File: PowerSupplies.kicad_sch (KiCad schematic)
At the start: 10 parts, among them U5 XL1509-3.3, U7 AP2112K-1.8

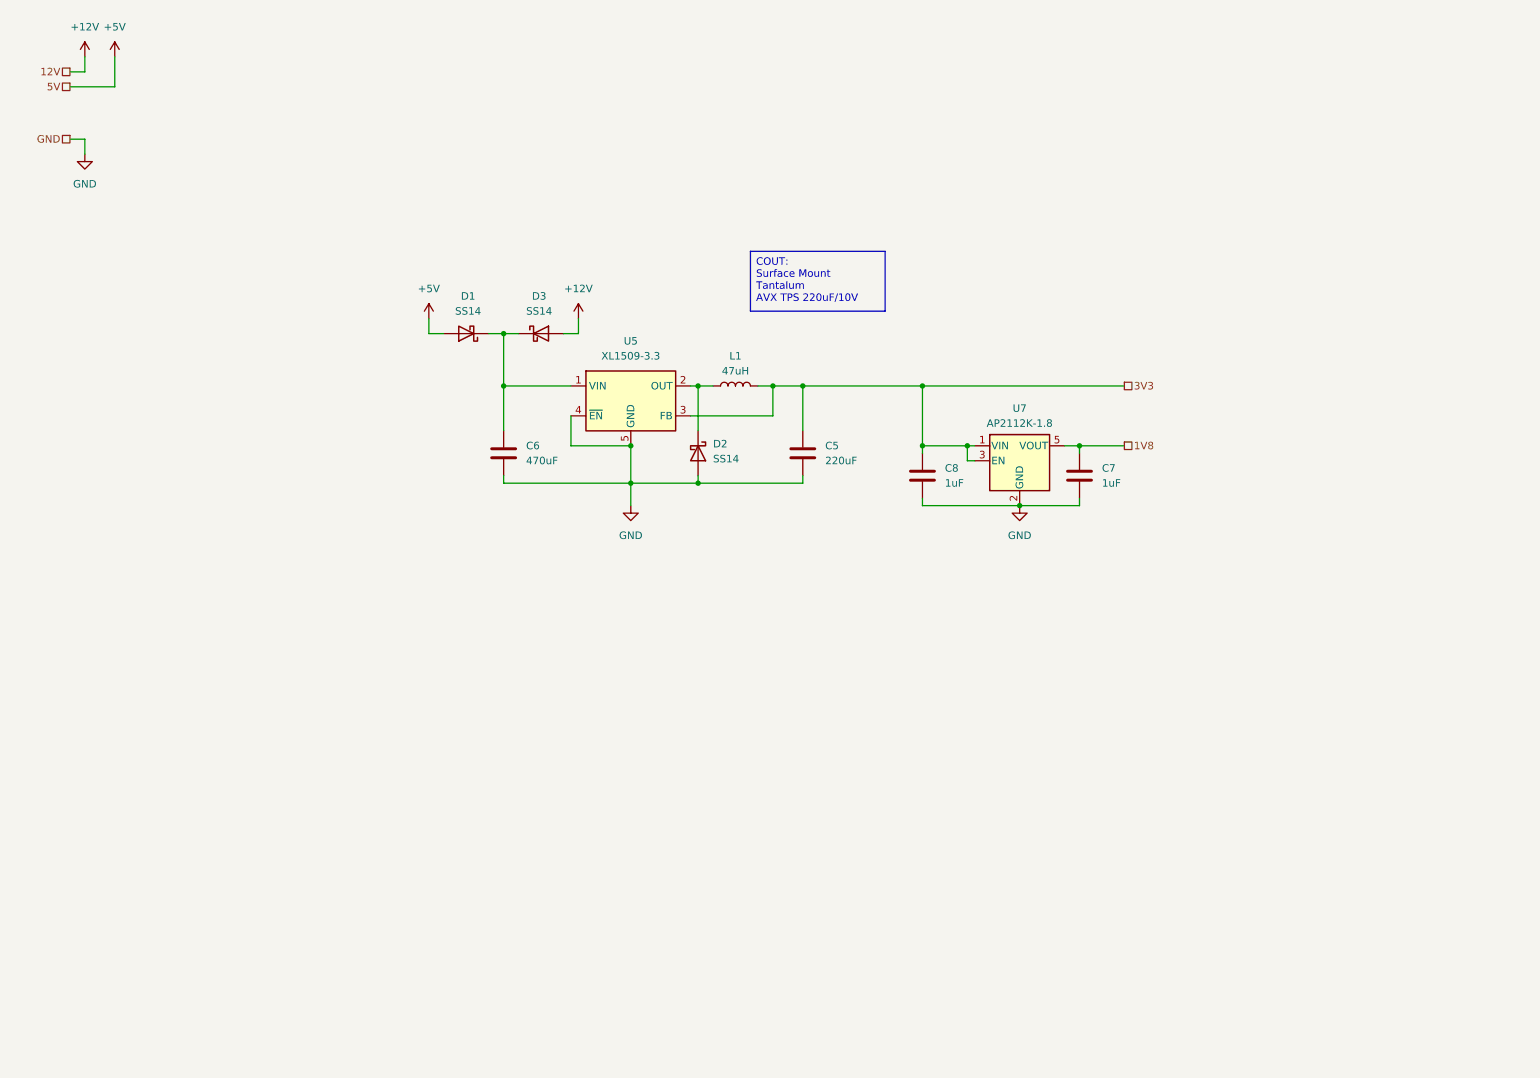
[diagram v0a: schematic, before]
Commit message: full initial power scheme
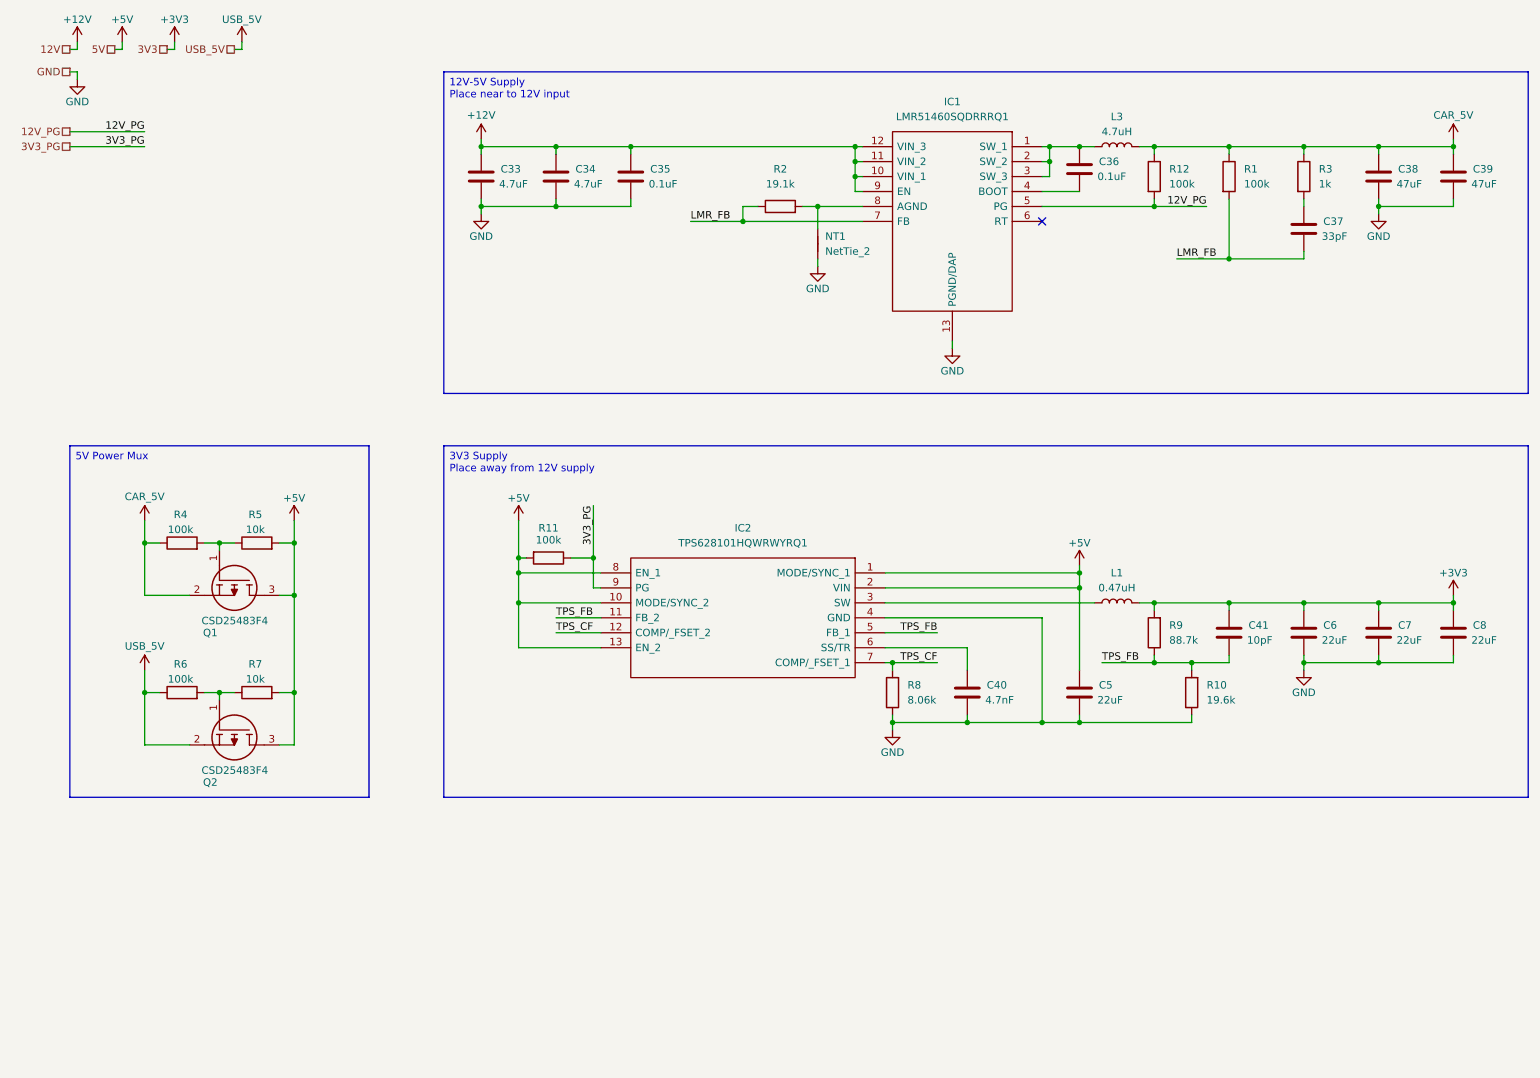
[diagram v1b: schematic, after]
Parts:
- removed D1, D2, D3: SS14, Diode_SMD:D_SMA, symbol Diode:SS14
- removed U5: XL1509-3.3, Package_SO:SOIC-8_3.9x4.9mm_P1.27mm, symbol Regulator_Switching:XL1509-3.3
- removed U7: AP2112K-1.8, Package_TO_SOT_SMD:SOT-23-5, symbol Regulator_Linear:AP2112K-1.8
- added C33, C34: 4.7uF, Capacitor_SMD:C_1210_3225Metric_Pad1.33x2.70mm_HandSolder, symbol Device:C
- added C35: 0.1uF, Capacitor_SMD:C_0603_1608Metric_Pad1.08x0.95mm_HandSolder, symbol Device:C
- added C36: 0.1uF, Capacitor_SMD:C_0402_1005Metric_Pad0.74x0.62mm_HandSolder, symbol Device:C
- added C37: 33pF, Capacitor_SMD:C_0402_1005Metric_Pad0.74x0.62mm_HandSolder, symbol Device:C
- added C38, C39: 47uF, Capacitor_SMD:C_1210_3225Metric_Pad1.33x2.70mm_HandSolder, symbol Device:C
- added C40: 4.7nF, Capacitor_SMD:C_0402_1005Metric_Pad0.74x0.62mm_HandSolder, symbol Device:C
- added C41: 10pF, Capacitor_SMD:C_0402_1005Metric_Pad0.74x0.62mm_HandSolder, symbol Device:C
- added IC1: LMR51460SQDRRRQ1, SON50P300X300X80-13N-D, symbol SamacSys_Parts:LMR51460SQDRRRQ1
- added IC2: TPS628101HQWRWYRQ1, SamacSys_Parts:TPS6281008QWRWYRQ1, symbol SamacSys_Parts:TPS62810QWRWYRQ1
- added L3: 4.7uH, Inductor_SMD:L_Coilcraft_XAL7030-472, symbol Device:L
- added NT1: NetTie_2, symbol Device:NetTie_2
- added Q1, Q2: CSD25483F4, SamacSys_Parts:CSD25483F4T, symbol SamacSys_Parts:CSD25483F4T
- added R1, R11, R12, R4, R6: 100k, Resistor_SMD:R_0402_1005Metric_Pad0.72x0.64mm_HandSolder, symbol Device:R
- added R10: 19.6k, Resistor_SMD:R_0402_1005Metric_Pad0.72x0.64mm_HandSolder, symbol Device:R
- added R2: 19.1k, Resistor_SMD:R_0402_1005Metric_Pad0.72x0.64mm_HandSolder, symbol Device:R
- added R3: 1k, Resistor_SMD:R_0402_1005Metric_Pad0.72x0.64mm_HandSolder, symbol Device:R
- added R5, R7: 10k, Resistor_SMD:R_0402_1005Metric_Pad0.72x0.64mm_HandSolder, symbol Device:R
- added R8: 8.06k, Resistor_SMD:R_0402_1005Metric_Pad0.72x0.64mm_HandSolder, symbol Device:R
- added R9: 88.7k, Resistor_SMD:R_0402_1005Metric_Pad0.72x0.64mm_HandSolder, symbol Device:R
- C5: value 220uF -> 22uF; footprint Capacitor_SMD:C_0603_1608Metric -> Inductor_SMD:L_1206_3216Metric_Pad1.22x1.90mm_HandSolder
- C6: value 470uF -> 22uF; footprint Capacitor_SMD:C_0603_1608Metric -> Inductor_SMD:L_1206_3216Metric_Pad1.22x1.90mm_HandSolder
- C7: value 1uF -> 22uF; footprint Capacitor_SMD:C_0603_1608Metric -> Inductor_SMD:L_1206_3216Metric_Pad1.22x1.90mm_HandSolder
- C8: value 1uF -> 22uF; footprint Capacitor_SMD:C_0603_1608Metric -> Capacitor_SMD:C_0603_1608Metric_Pad1.08x0.95mm_HandSolder
- L1: value 47uH -> 0.47uH; footprint Inductor_SMD:L_Sunlord_SWPA4030S -> INDPM7066X240N
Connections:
- net 1V8 is gone; now on net +3V3: C7.1
- net +12V: now also C33.1, C34.1, C35.1, IC1.10 (VIN_1), IC1.11 (VIN_2), IC1.12 (VIN_3), IC1.9 (EN)
- net +5V: now also C5.1, IC2.1 (MODE/SYNC_1), IC2.10 (MODE/SYNC_2), IC2.13 (EN_2), IC2.2 (VIN), IC2.8 (EN_1), Q1.3, Q2.3, R11.2, R5.2, R7.2
- net GND: now also C33.2, C34.2, C35.2, C38.2, C39.2, C40.2, IC1.13 (PGND/DAP), IC2.4 (GND), NT1.1, R10.1, R8.1
- net +3V3: now reaches C6.1
- net +3V3: now also C8.1, L1.2, C41.1, R9.2
- net at L1.1: now also IC2.3 (SW)
- removed net 3V3: C5.1, C8.1, L1.2
- new net: Q2.1, R6.2, R7.1
- new net: C37.1, R3.2
- new net: IC1.8 (AGND), NT1.2, R2.2
- new net: Q1.1, R4.2, R5.1
- new net: C36.1, IC1.1 (SW_1), IC1.2 (SW_2), IC1.3 (SW_3), L3.1
- new net: C36.2, IC1.4 (BOOT)
- new net: C40.1, IC2.6 (SS/TR)
- new net 12V_PG: IC1.5 (PG), R12.2
- new net 3V3_PG: IC2.9 (PG), R11.1
- new net CAR_5V: C38.1, C39.1, L3.2, Q1.2, R1.1, R12.1, R3.1, R4.1
- new net LMR_FB: C37.2, IC1.7 (FB), R1.2, R2.1
- new net TPS_CF: IC2.12 (COMP/_FSET_2), IC2.7 (COMP/_FSET_1), R8.2
- new net TPS_FB: C41.2, IC2.11 (FB_2), IC2.5 (FB_1), R10.2, R9.1
- new net USB_5V: Q2.2, R6.1
- no-connect marks 0 -> 1

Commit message: improved power supplies, added ADCs
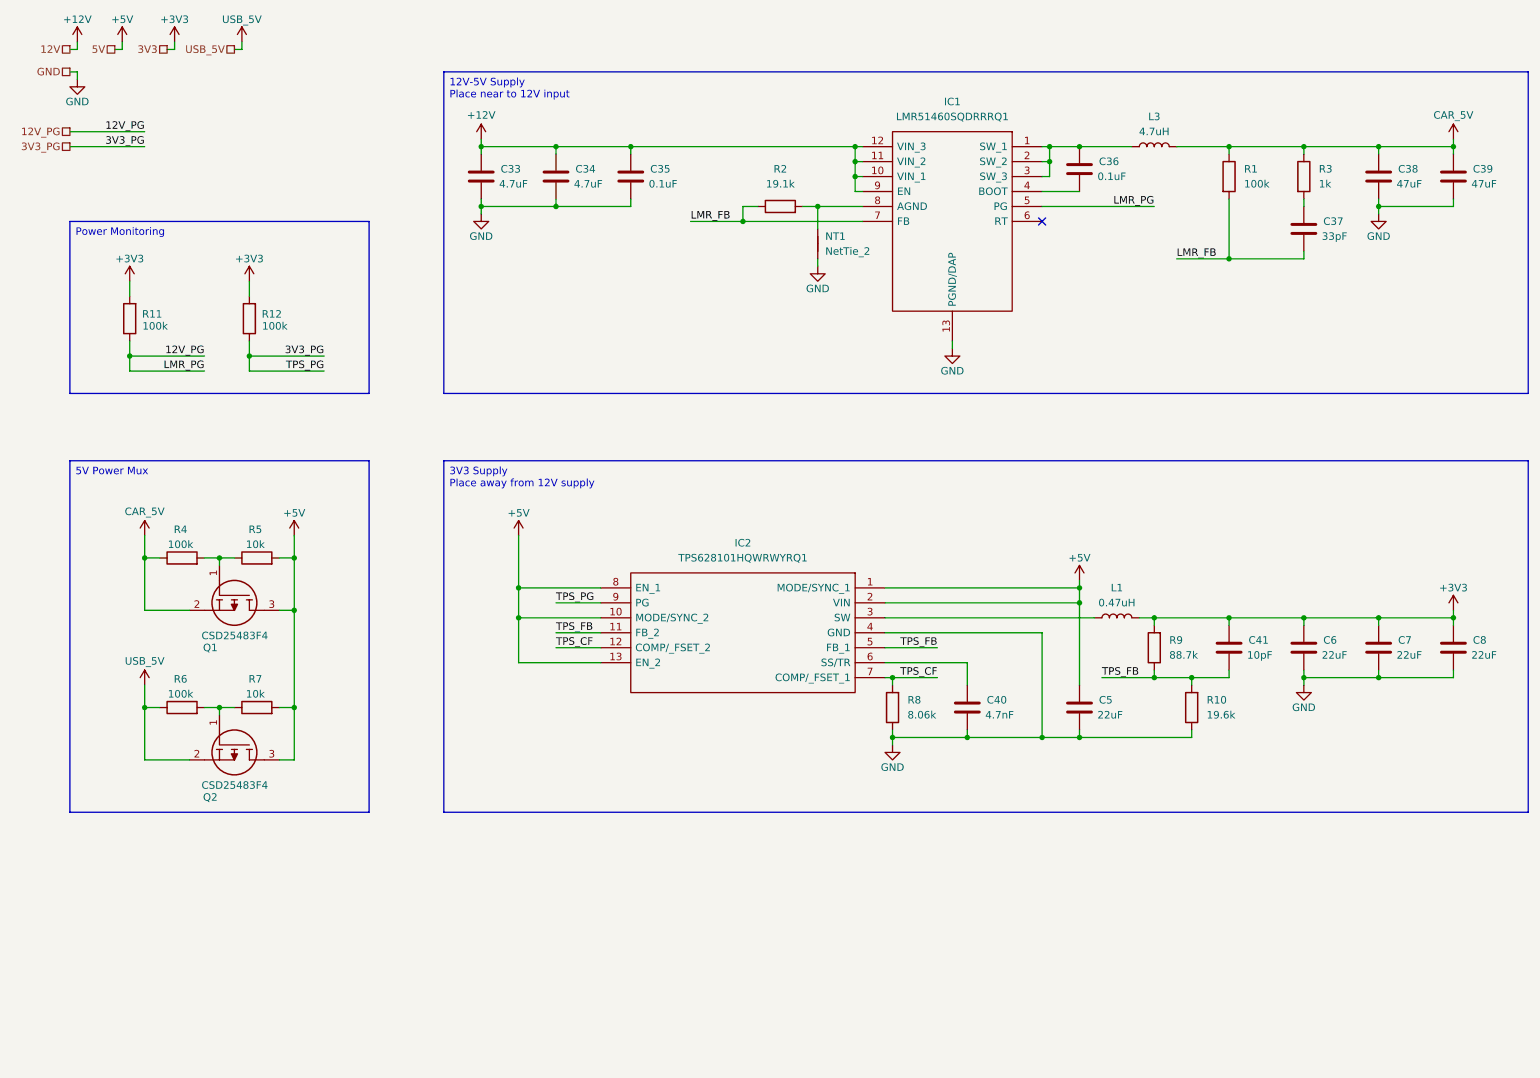
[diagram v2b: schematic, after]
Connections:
- net +3V3: now also R11.2, R12.2
- net +5V: no longer R11.2
- net 12V_PG: now also R11.1; no longer R12.2
- net 3V3_PG: now also R12.1; no longer R11.1
- net CAR_5V: no longer R12.1
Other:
- moved on the sheet: C40, C41, C5, C6, C7, C8, IC2, L1, L3, Q1, Q2, R10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

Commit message: wip
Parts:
- NT1: footprint (none) -> NetTie:NetTie-2_SMD_Pad0.5mm
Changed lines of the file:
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@@
 			)
 		)
-		(property "Footprint" ""
+		(property "Footprint" "NetTie:NetTie-2_SMD_Pad0.5mm"
 			(at 152.4 54.61 0)
 			(effects

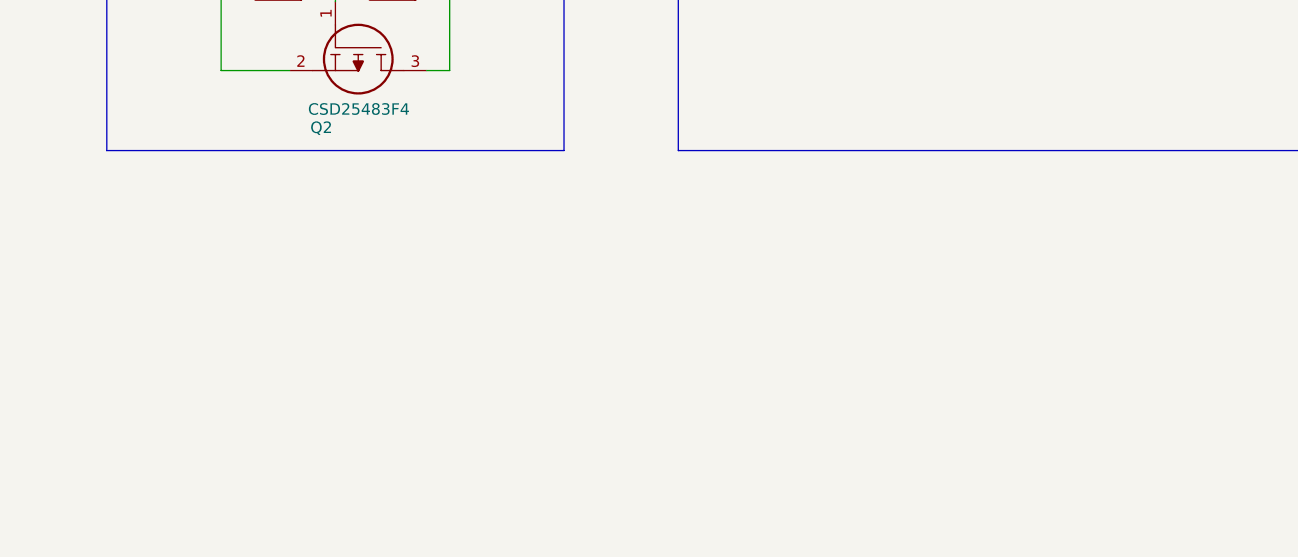
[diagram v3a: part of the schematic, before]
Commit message: routed more sheets, improved analogs. next 5v /analog ground
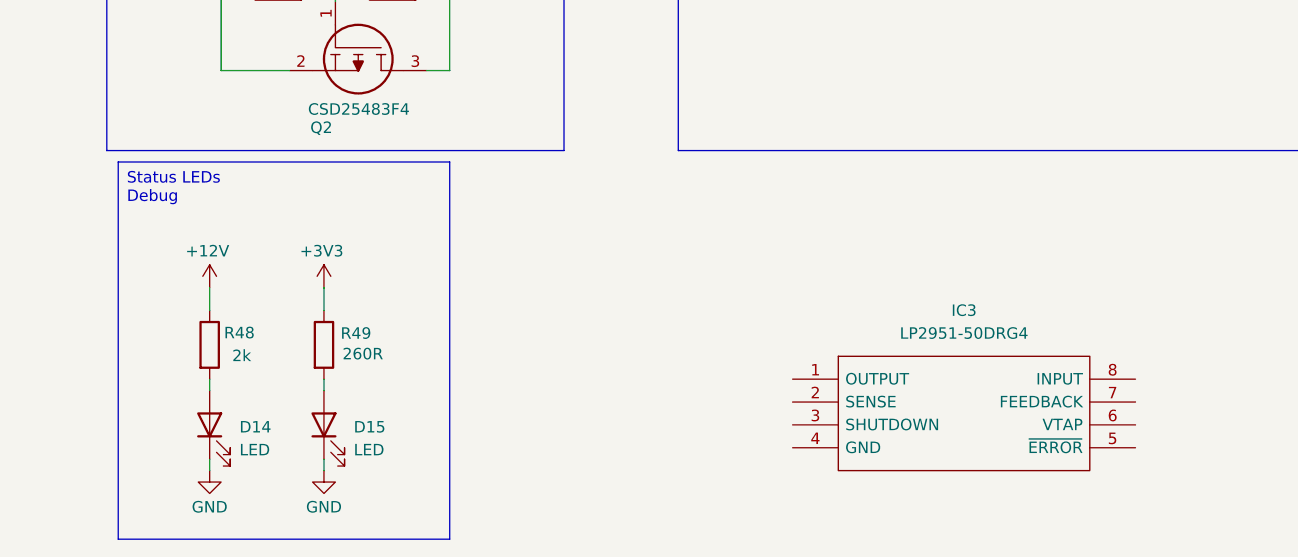
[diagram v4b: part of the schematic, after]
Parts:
- added D14, D15: LED, LED_SMD:LED_0603_1608Metric_Pad1.05x0.95mm_HandSolder, symbol Device:LED
- added IC3: LP2951-50DRG4, SOIC127P600X175-8N, symbol 0_SamacSys_Parts:LP2951-50DRG4
- added R48: 2k, Resistor_SMD:R_0603_1608Metric_Pad0.98x0.95mm_HandSolder, symbol Device:R
- added R49: 260R, Resistor_SMD:R_0603_1608Metric_Pad0.98x0.95mm_HandSolder, symbol Device:R
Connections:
- net +12V: now also R48.1
- net +3V3: now also R49.1
- net GND: now also D14.1 (K), D15.1 (K)
- new net: D15.2 (A), R49.2
- new net: D14.2 (A), R48.2
